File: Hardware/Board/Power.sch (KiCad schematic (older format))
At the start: 86 parts, among them Q100 2N7002, Q102 2N7002, Q103 2N7002, Q104 2N7002, U100 MAX17572, U101 MAX17572, U102 MAX17572, U104 MAX17574, U105 MAX17574

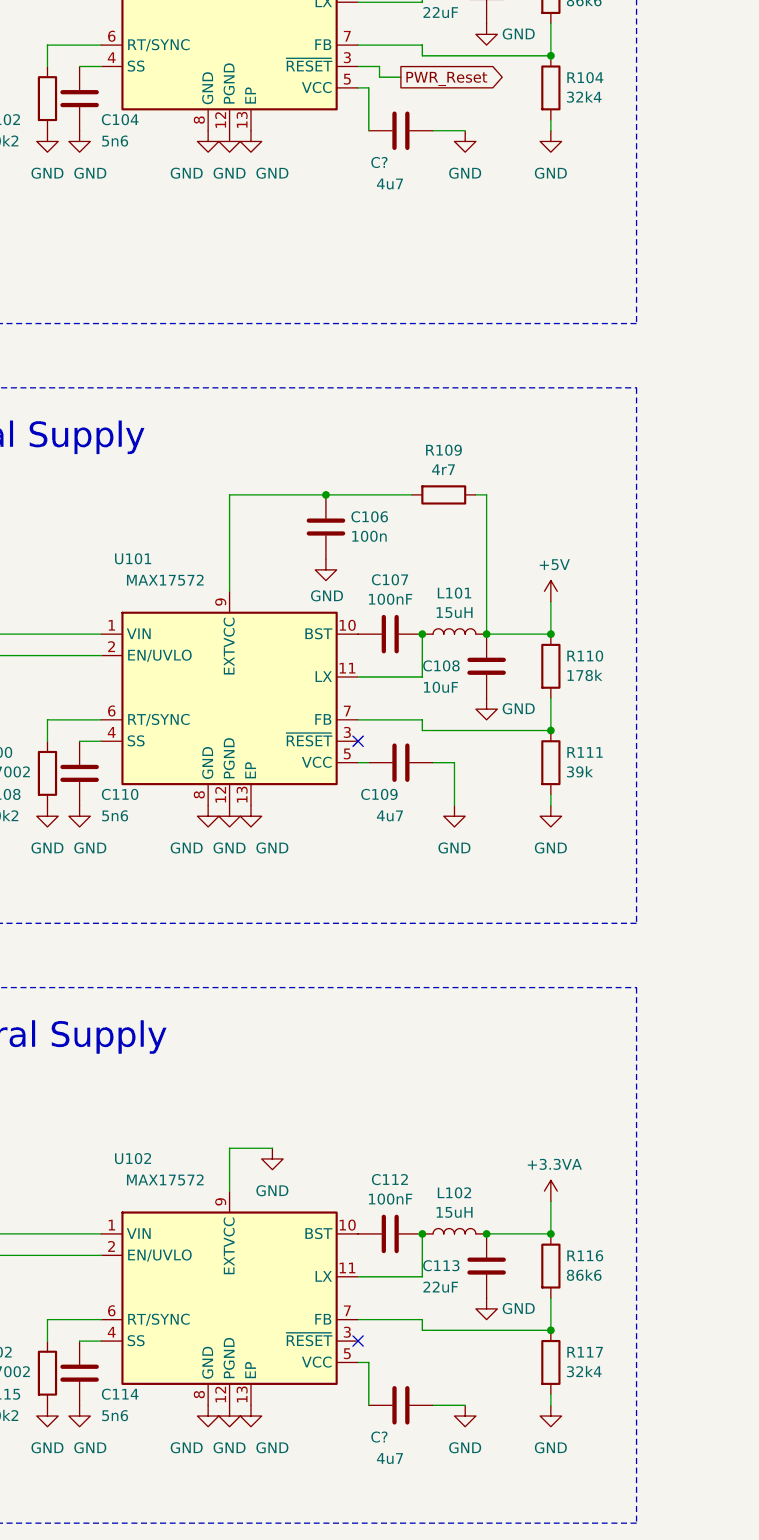
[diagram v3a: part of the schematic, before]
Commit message: Layout Fehler beseitigt
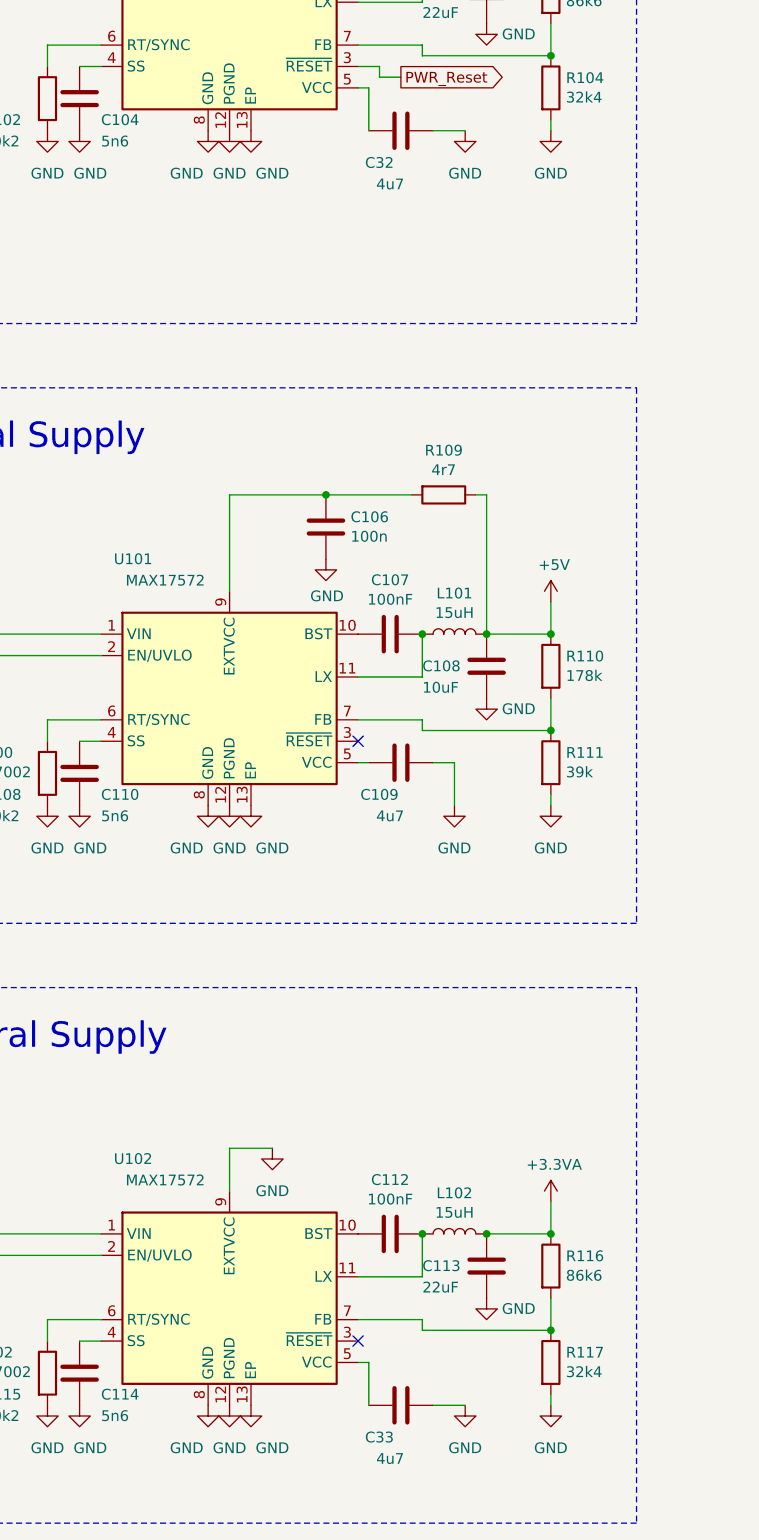
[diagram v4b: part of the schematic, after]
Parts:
- gave numbers to parts that had none: 2
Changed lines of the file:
@@
 $EndComp
 $Comp
-L Womo-rescue:C-Device C?
+L Womo-rescue:C-Device C32
 U 1 1 5E15C6EC
 P 4400 2400
-AR Path="/5C8BBC9A/5E15C6EC" Ref="C?"  Part="1"
+AR Path="/5C8BBC9A/5E15C6EC" Ref="C32"  Part="1"
 AR Path="/5E0C5EEA/5E15C6EC" Ref="C?"  Part="1"
-F 0 "C?" V 4550 2300 50  0000 C CNN
+F 0 "C32" V 4550 2300 50  0000 C CNN
 F 1 "4u7" V 4650 2350 50  0000 C CNN
 F 2 "Capacitor_SMD:C_0603_1608Metric" H 4438 2250 50  0001 C CNN
@@
 $EndComp
 $Comp
-L Womo-rescue:C-Device C?
+L Womo-rescue:C-Device C33
 U 1 1 5E19DC38
 P 4400 8350
-AR Path="/5C8BBC9A/5E19DC38" Ref="C?"  Part="1"
+AR Path="/5C8BBC9A/5E19DC38" Ref="C33"  Part="1"
 AR Path="/5E0C5EEA/5E19DC38" Ref="C?"  Part="1"
-F 0 "C?" V 4550 8250 50  0000 C CNN
+F 0 "C33" V 4550 8250 50  0000 C CNN
 F 1 "4u7" V 4650 8300 50  0000 C CNN
 F 2 "Capacitor_SMD:C_0603_1608Metric" H 4438 8200 50  0001 C CNN

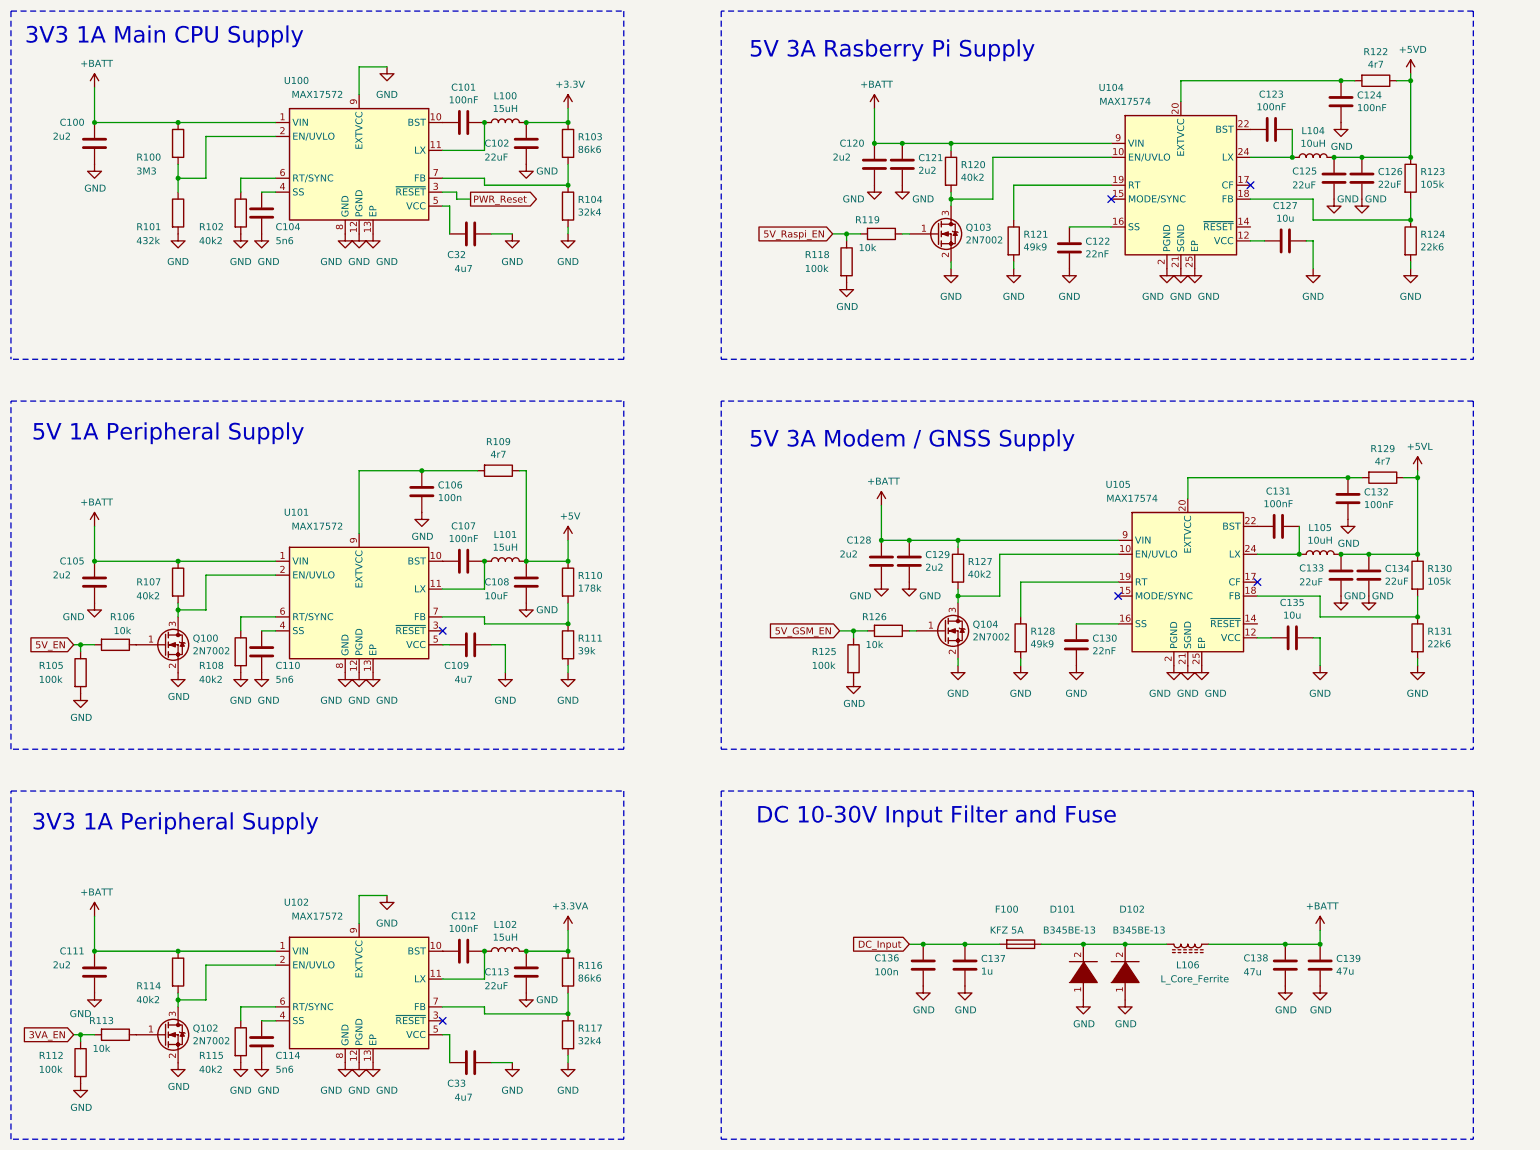
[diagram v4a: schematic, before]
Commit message: Displayunit: Kleiner Fix Mainboard: Netzteil Sektion komplett auf TI umgestellt, Footprints angepasst. Victron kompatible TTY Ports platziert und gerouted, auf Version 2.0 gehoben.
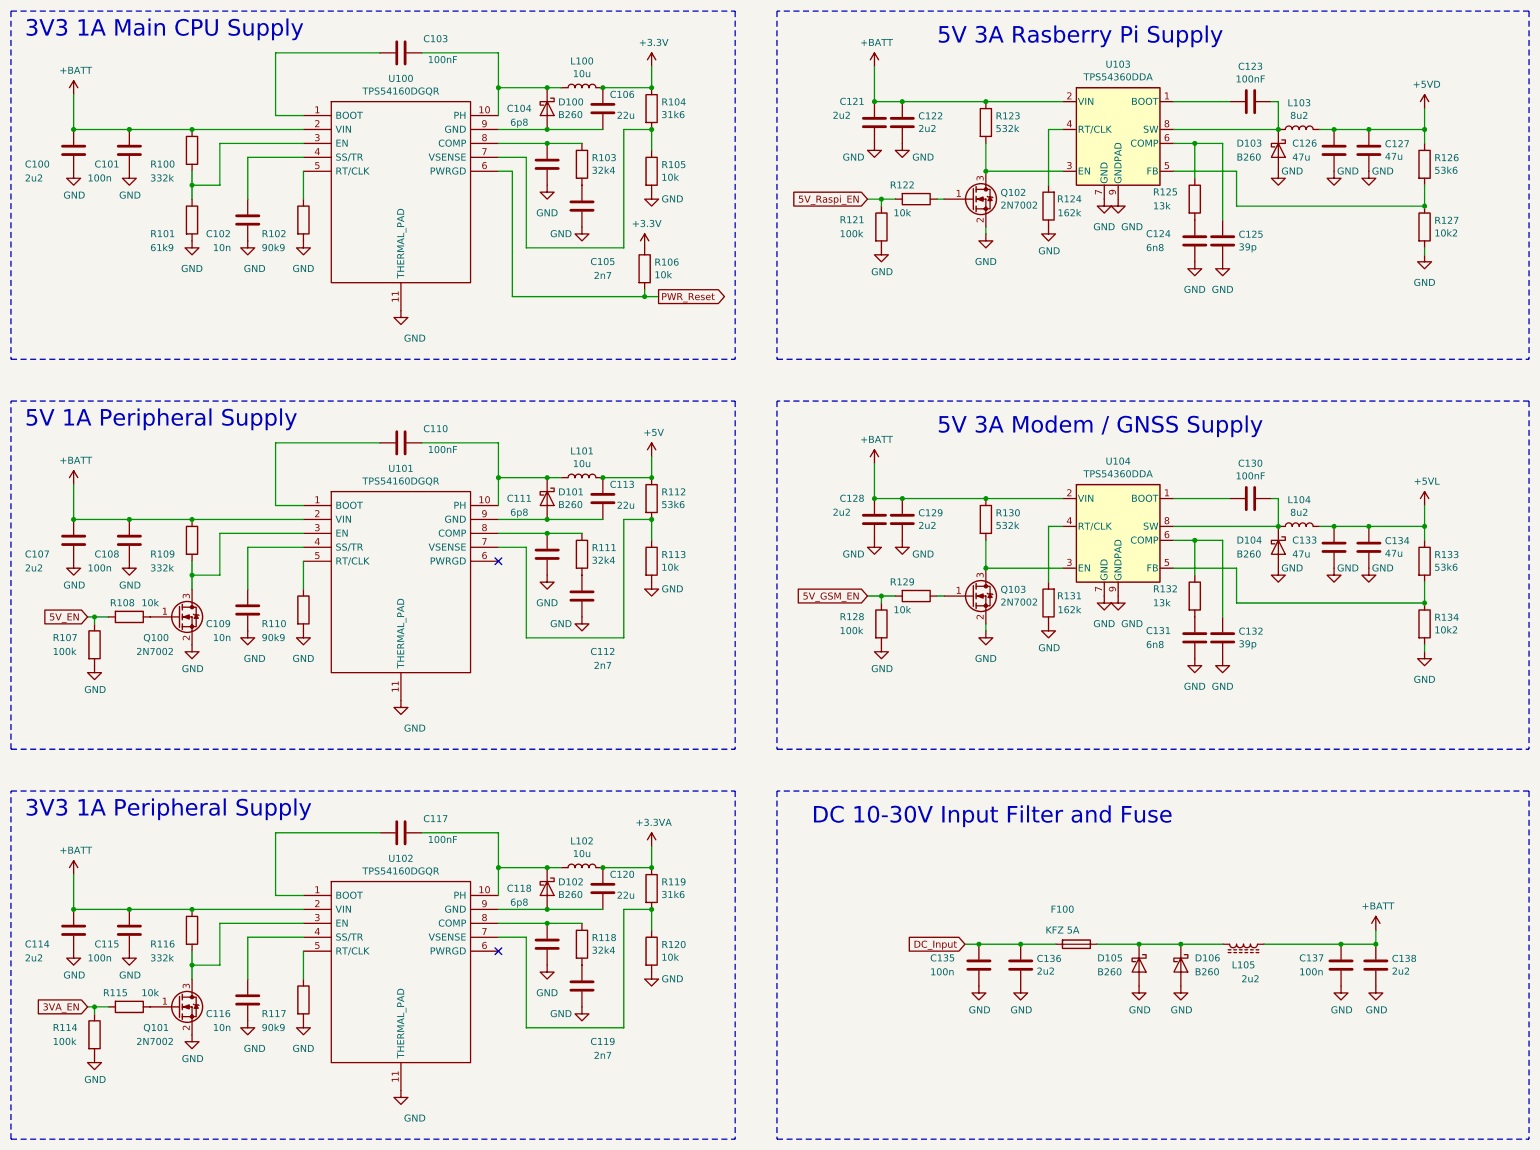
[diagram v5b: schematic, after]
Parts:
- removed C106: 100n, Capacitor_SMD:C_0603_1608Metric, symbol Womo-rescue:C-Device
- removed C127, C135: 10u, Capacitor_SMD:C_1210_3225Metric, symbol Womo-rescue:C-Device
- removed C33: 4u7, Capacitor_SMD:C_0603_1608Metric, symbol Womo-rescue:C-Device
- removed D101, D102: B345BE-13, Diode_SMD:D_SMB, symbol Womo-rescue:DIODE-pspice
- removed L105: 10uH, Womo-Lin:XAL8080, symbol Womo-rescue:L-Device
- removed Q102, Q104: 2N7002, Package_TO_SOT_SMD:SOT-23, symbol Womo-rescue:2N7002-Transistor_FET
- removed R107, R108, R127: 40k2, Resistor_SMD:R_0603_1608Metric, symbol Womo-rescue:R-Device
- removed R125: 100k, Resistor_SMD:R_0603_1608Metric, symbol Womo-rescue:R-Device
- removed R126: 10k, Resistor_SMD:R_0603_1608Metric, symbol Womo-rescue:R-Device
- removed U100, U101, U102: MAX17572, Package_DFN_QFN:DFN-12-1EP_3x3mm_P0.5mm_EP2.05x2.86mm, symbol Womo-rescue:MAX17572-Regulator_Switching
- removed U104, U105: MAX17574, Package_DFN_QFN:QFN-24-1EP_4x5mm_P0.5mm_EP2.65x3.65mm, symbol Womo-rescue:MAX17574-Regulator_Switching
- added C101, C115: 100n, Capacitor_SMD:C_0603_1608Metric, symbol Womo-rescue:C-Device
- added C116: 10n, Capacitor_SMD:C_0603_1608Metric, symbol Womo-rescue:C-Device
- added C117: 100nF, Capacitor_SMD:C_0603_1608Metric, symbol Womo-rescue:C-Device
- added C118: 6p8, Capacitor_SMD:C_0603_1608Metric, symbol Womo-rescue:C-Device
- added C119: 2n7, Capacitor_SMD:C_0603_1608Metric, symbol Womo-rescue:C-Device
- added C120: 22u, Capacitor_SMD:C_1210_3225Metric, symbol Womo-rescue:C-Device
- added D100, D101, D102, D103, D104, D105, D106: B260, Diode_SMD:D_SMB, symbol Diode:B260
- added L104: 8u2, Womo-Lin:XAL8080, symbol Womo-rescue:L-Device
- added Q101, Q103: 2N7002, Package_TO_SOT_SMD:SOT-23, symbol Womo-rescue:2N7002-Transistor_FET
- added R103, R118: 32k4, Resistor_SMD:R_0603_1608Metric, symbol Womo-rescue:R-Device
- added R106, R120: 10k, Resistor_SMD:R_0603_1608Metric, symbol Womo-rescue:R-Device
- added R119: 31k6, Resistor_SMD:R_0603_1608Metric, symbol Womo-rescue:R-Device
- added R132: 13k, Resistor_SMD:R_0603_1608Metric, symbol Womo-rescue:R-Device
- added R133: 53k6, Resistor_SMD:R_0603_1608Metric, symbol Womo-rescue:R-Device
- added R134: 10k2, Resistor_SMD:R_0603_1608Metric, symbol Womo-rescue:R-Device
- added U100, U101, U102: TPS54160DGQR, Womo-Lin:SOP50P490X110-11N, symbol Womo-Lin:TPS54160DGQR
- added U103, U104: TPS54360DDA, Package_SO:TI_SO-PowerPAD-8_ThermalVias, symbol Regulator_Switching:TPS54340DDA
- C102: renamed from C104; value 5n6 -> 10n
- C104: renamed from C32; value 4u7 -> 6p8
- C105: value 2u2 -> 2n7; footprint Capacitor_SMD:C_1210_3225Metric -> Capacitor_SMD:C_0603_1608Metric
- C106: renamed from C102; value 22uF -> 22u
- C107: value 100nF -> 2u2; footprint Capacitor_SMD:C_0603_1608Metric -> Capacitor_SMD:C_1210_3225Metric
- C108: value 10uF -> 100n; footprint Capacitor_SMD:C_1210_3225Metric -> Capacitor_SMD:C_0603_1608Metric
- C109: value 4u7 -> 10n
- C110: value 5n6 -> 100nF
- C111: value 2u2 -> 6p8; footprint Capacitor_SMD:C_1210_3225Metric -> Capacitor_SMD:C_0603_1608Metric
- C112: value 100nF -> 2n7
- C113: value 22uF -> 22u
- C114: value 5n6 -> 2u2; footprint Capacitor_SMD:C_0603_1608Metric -> Capacitor_SMD:C_1210_3225Metric
- C124, C131: value 100nF -> 6n8
- C125: renamed from C122; value 22nF -> 39p
- C126: renamed from C125; value 22uF -> 47u
- C127: renamed from C126; value 22uF -> 47u
- C130: value 22nF -> 100nF
- C132: value 100nF -> 39p
- C133, C134: value 22uF -> 47u
- C136: renamed from C137; value 1u -> 2u2
- C137: renamed from C138; value 47u -> 100n; footprint Capacitor_SMD:C_1210_3225Metric -> Capacitor_SMD:C_0603_1608Metric
- C138: renamed from C139; value 47u -> 2u2
- L100, L101, L102: value 15uH -> 10u
- L103: renamed from L104; value 10uH -> 8u2
- L105: renamed from L106; value L_Core_Ferrite -> 2u2
- R100: value 3M3 -> 332k
- R101: value 432k -> 61k9
- R102: value 40k2 -> 90k9
- R104: renamed from R103; value 86k6 -> 31k6
- R105: renamed from R104; value 32k4 -> 10k
- R109: value 4r7 -> 332k
- R110: value 178k -> 90k9
- R111: value 39k -> 32k4
- R112: value 100k -> 53k6
- R114: value 40k2 -> 100k
- R115: value 40k2 -> 10k
- R116: value 86k6 -> 332k
- R117: value 32k4 -> 90k9
- R123: renamed from R120; value 40k2 -> 532k
- R124: renamed from R122; value 4r7 -> 162k
- R125: renamed from R121; value 49k9 -> 13k
- R126: renamed from R123; value 105k -> 53k6
- R127: renamed from R124; value 22k6 -> 10k2
- R128: value 49k9 -> 100k
- R129: value 4r7 -> 10k
- R130: value 105k -> 532k
- R131: value 22k6 -> 162k
- renumbered C101 to C103, C120 to C121, C121 to C122, C136 to C135, Q103 to Q102, R105 to R107, R106 to R108, R118 to R121, R119 to R122
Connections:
- net +3.3VA: now also C120.1, R119.1; no longer C113.1, R116.1
- net +3V3: now also R106.1
- net +5V: now also C113.1, R112.1; no longer C108.1, R109.1, R110.1
- net +5VD: no longer R124.1
- net +5VL: now also L104.2, R133.1; no longer R129.1, R130.1
- net +BATT: now also C107.1, C108.1, C114.1, R109.1, R116.1, R130.1, C101.1, C115.1, U100.2 (VIN), U101.2 (VIN), U102.2 (VIN), U103.2 (VIN), U104.2 (VIN); no longer C105.1, C111.1, R114.1
- net 3VA_EN: now also R114.1, R115.2; no longer R112.1, R113.2
- net 5V_GSM_EN: now also R128.1, R129.2
- net GND: now also C105.1, C107.2, C109.2, C111.1, C112.1, C131.2, R110.2, R113.2, R114.2, R124.1, R131.1, C101.2, C115.2, C116.2, C118.1, C119.1, D103.2 (A), D104.2 (A), D105.2 (A), D106.2 (A), Q101.2 (S), Q103.2 (S), R120.2, R134.2, U100.11 (THERMAL_PAD), U101.11 (THERMAL_PAD), U102.11 (THERMAL_PAD), U103.7 (GND), U103.9 (GNDPAD), U104.7 (GND), U104.9 (GNDPAD); no longer C105.2, C106.2, C109.1, C110.2, C111.2, C113.2, C130.2, R111.2, R112.2, R115.2, R125.2, R131.2
- net PWR_Reset: now also R106.2, U100.6 (PWRGD)
- net at C103.2: now also U100.1 (BOOT)
- net at C103.1, L100.1: now also D100.1 (K), U100.10 (PH)
- net at R100.2, R101.1: now also U100.3 (EN)
- net at C102.1: now also U100.4 (SS/TR)
- net at C104.2: now also R103.1, U100.8 (COMP)
- net at R102.1: now also U100.5 (RT/CLK)
- net at R104.2, R105.1: now also U100.7 (VSENSE)
- net at L101.1: now also C110.1, D101.1 (K), U101.10 (PH); no longer C107.1
- net at Q100.3 (D): now also R109.2, U101.3 (EN)
- net at R111.1: now also C111.2, U101.8 (COMP); no longer R110.2
- net at C112.2: now also R111.2
- net at L102.1: now also C117.1, D102.1 (K), U102.10 (PH); no longer C112.1
- net at R115.1: now also Q101.1 (G)
- net at R116.2: now also Q101.3 (D), U102.3 (EN); no longer R117.1
- net at C123.1, L103.1: now also D103.1 (K), U103.8 (SW)
- net at Q102.3 (D), R123.2: now also U103.3 (EN)
- net at C125.1: now also R125.1, U103.6 (COMP)
- net at R126.2, R127.1: now also U103.5 (FB)
- net at C124.1: now also R125.2; no longer R124.2
- net at C123.2: now also U103.1 (BOOT)
- net at R113.1: now also R112.2, U101.7 (VSENSE)
- net at F100.1, L105.2: now also D105.1 (K), D106.1 (K)
- net at C131.1: now also R132.2
- net at C130.1: now also D104.1 (K), L104.1, U104.8 (SW)
- net at R130.2: now also Q103.3 (D), U104.3 (EN); no longer R131.1
- net at C132.1: now also R132.1, U104.6 (COMP); no longer R129.2
- new net: R124.2, U103.4 (RT/CLK)
- new net: C106.2, D100.2 (A), U100.9 (GND)
- new net: C105.2, R103.2
- new net: C113.2, D101.2 (A), U101.9 (GND)
- new net: C110.2, U101.1 (BOOT)
- new net: C109.1, U101.4 (SS/TR)
- new net: R110.1, U101.5 (RT/CLK)
- new net: C130.2, U104.1 (BOOT)
- new net: R133.2, R134.1, U104.5 (FB)
- new net: Q103.1 (G), R129.1
- new net: R131.2, U104.4 (RT/CLK)
- new net: C119.2, R118.2
- new net: C118.2, R118.1, U102.8 (COMP)
- new net: C120.2, D102.2 (A), U102.9 (GND)
- new net: C117.2, U102.1 (BOOT)
- new net: C116.1, U102.4 (SS/TR)
- new net: R117.1, U102.5 (RT/CLK)
- new net: R119.2, R120.1, U102.7 (VSENSE)
- no-connect marks 6 -> 2
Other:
- moved on the sheet: C100, C102, C103, C104, C106, C121, C122, C123, C124, C125, C126, C127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
